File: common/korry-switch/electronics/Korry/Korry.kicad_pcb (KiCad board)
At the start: 2 copper layers, 20.5 x 20.5 mm, 11 parts, among them J1 Conn_01x02_Pin, J2 Conn_01x04_Pin

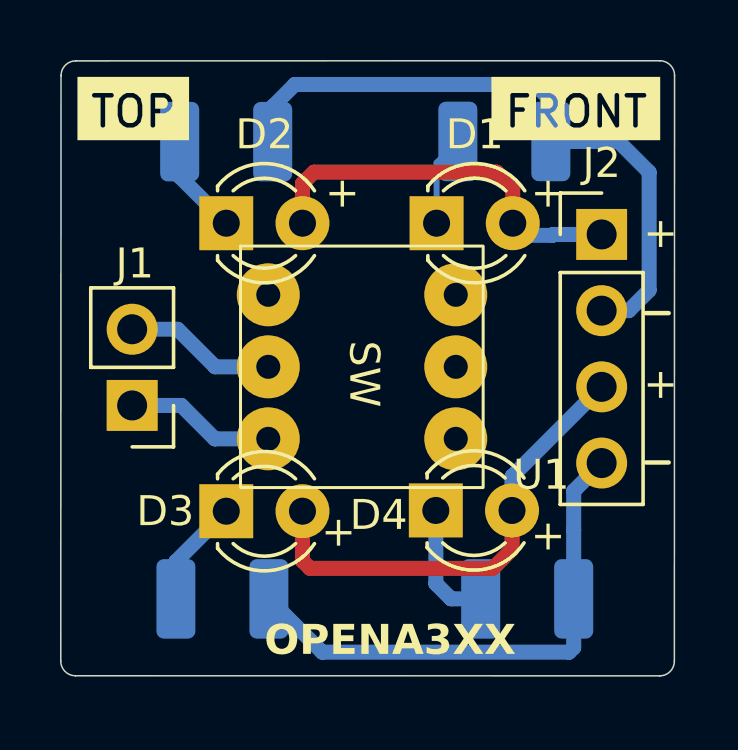
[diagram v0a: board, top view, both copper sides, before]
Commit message: Added Mantoga credits
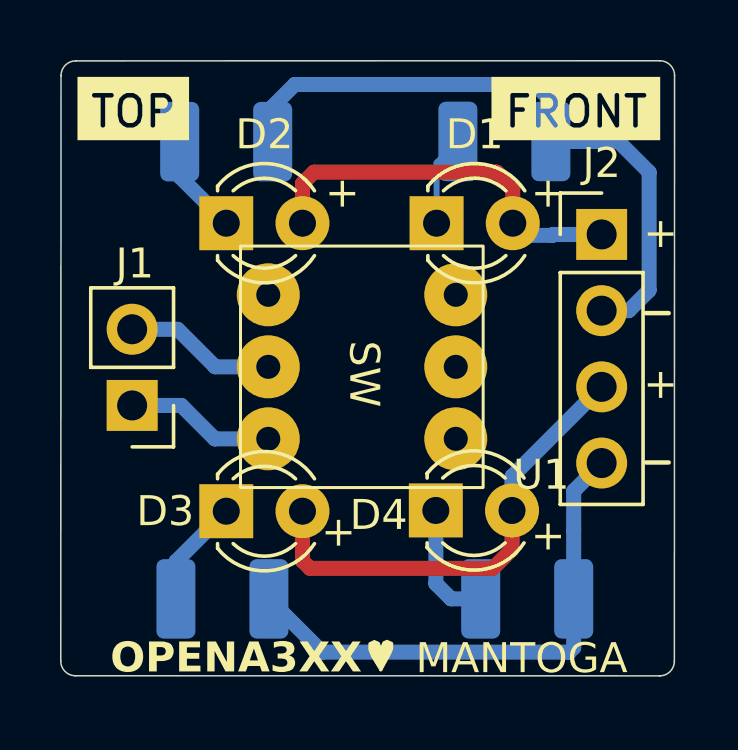
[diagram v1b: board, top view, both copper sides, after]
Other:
- board text added: "MANTOGA"
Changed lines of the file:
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@@
 			)
 		)
+		(property "LCSC" "C2935910"
+			(at 0 0 0)
+			(layer "F.SilkS")
+			(hide yes)
+			(effects
+				(font
+					(size 1.27 1.27)
+					(thickness 0.15)
+				)
+			)
+		)
 		(property ki_fp_filters "Connector*:*_1x??_*")
 		(sheetname "/")
@@
 			)
 		)
+		(property "LCSC" "C2905434"
+			(at 0 0 0)
+			(layer "F.SilkS")
+			(hide yes)
+			(effects
+				(font
+					(size 1.27 1.27)
+					(thickness 0.15)
+				)
+			)
+		)
 		(property ki_fp_filters "Connector*:*_1x??_*")
 		(sheetname "/")
@@
 			)
 		)
+		(property "LCSC" "C2933866"
+			(at 0 0 0)
+			(layer "B.SilkS")
+			(hide yes)
+			(effects
+				(font
+					(size 1.27 1.27)
+					(thickness 0.15)
+				)
+			)
+		)
 		(property ki_fp_filters "R_*")
 		(sheetname "/")
@@
 			)
 		)
+		(property "LCSC" "C2933866"
+			(at 0 0 0)
+			(layer "B.SilkS")
+			(hide yes)
+			(effects
+				(font
+					(size 1.27 1.27)
+					(thickness 0.15)
+				)
+			)
+		)
 		(property ki_fp_filters "R_*")
 		(sheetname "/")
@@
 			)
 		)
+		(property "LCSC" "C2933866"
+			(at 0 0 0)
+			(layer "B.SilkS")
+			(hide yes)
+			(effects
+				(font
+					(size 1.27 1.27)
+					(thickness 0.15)
+				)
+			)
+		)
 		(property ki_fp_filters "R_*")
 		(sheetname "/")
@@
 			)
 		)
+		(property "LCSC" "C2933866"
+			(at 0 0 0)
+			(layer "B.SilkS")
+			(hide yes)
+			(effects
+				(font
+					(size 1.27 1.27)
+					(thickness 0.15)
+				)
+			)
+		)
 		(property ki_fp_filters "R_*")
 		(sheetname "/")
@@
 		(layer "B.Mask")
 	)
+	(gr_poly
+		(pts
+			(xy 70.66 66.795) (xy 71.18 66.795) (xy 70.93 67.215)
+		)
+		(stroke
+			(width 0.1)
+			(type solid)
+		)
+		(fill yes)
+		(layer "F.SilkS")
+	)
 	(gr_line
 		(start 79.773294 60.3504)
@@
 		(layer "F.SilkS")
 	)
+	(gr_line
+		(start 70.94 67.265)
+		(end 71.2 66.785)
+		(stroke
+			(width 0.1)
+			(type default)
+		)
+		(layer "F.SilkS")
+	)
 	(gr_poly
 		(pts
@@
 		(layer "F.SilkS")
 	)
+	(gr_line
+		(start 70.66 66.795)
+		(end 70.94 67.265)
+		(stroke
+			(width 0.1)
+			(type default)
+		)
+		(layer "F.SilkS")
+	)
+	(gr_poly
+		(pts
+			(xy 70.66 66.795) (xy 70.57 66.585236) (xy 70.57272 66.39019) (xy 70.724217 66.318898) (xy 70.86 66.38)
+			(xy 70.94 66.62) (xy 71.036977 66.361395) (xy 71.145626 66.31125) (xy 71.304332 66.382925) (xy 71.3 66.57)
+			(xy 71.21 66.775)
+		)
+		(stroke
+			(width 0.1)
+			(type solid)
+		)
+		(fill yes)
+		(layer "F.SilkS")
+	)
 	(gr_poly
 		(pts
@@
 	)
 	(gr_text "OPENA3XX"
-		(at 67.056 66.8528 0)
+		(at 61.92 67.44 0)
 		(layer "F.SilkS")
 		(effects
@@
 		)
 	)
+	(gr_text "MANTOGA"
+		(at 72.1 67.461819 0)
+		(layer "F.SilkS")
+		(effects
+			(font
+				(size 1 1)
+				(thickness 0.15)
+			)
+			(justify left bottom)
+		)
+	)
